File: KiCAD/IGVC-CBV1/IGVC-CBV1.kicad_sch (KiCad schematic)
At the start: 42 parts, among them IC1 SPX3819M5-L-3-3_TR, IC1 STM32F407ZGT6, IC3 AT45DB081E-SSHN-B, J1 12401948E412A, J1 STLINKV2 PINS (2.54mm Pitch), J2 Motor Driver Pins (2.54mm Pit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, J4 Conn_01x02, SW1 SW_SPDT, Y1 EB2532YA12-25.000M_TR

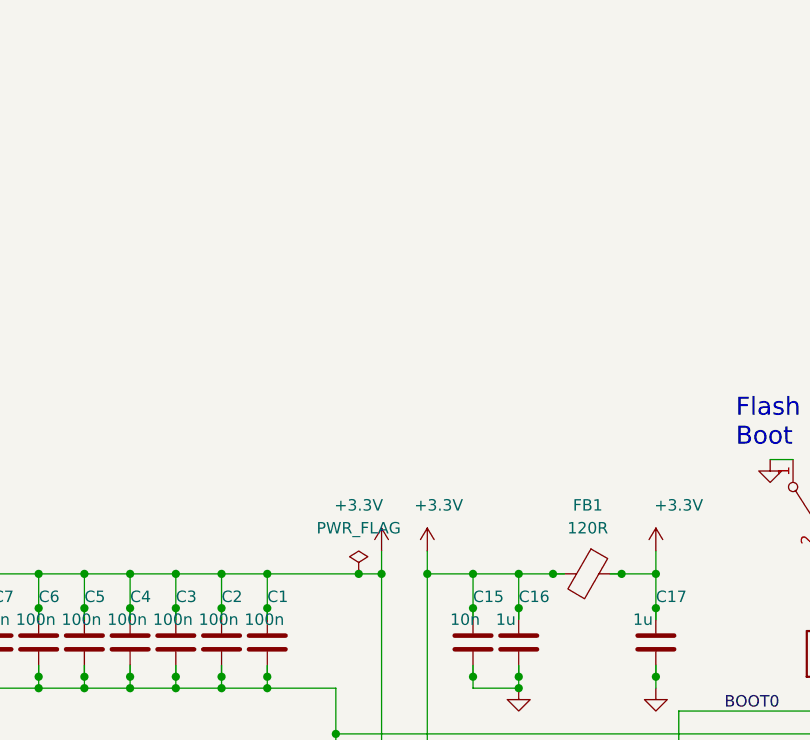
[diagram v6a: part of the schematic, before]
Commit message: Finished PCB Traces
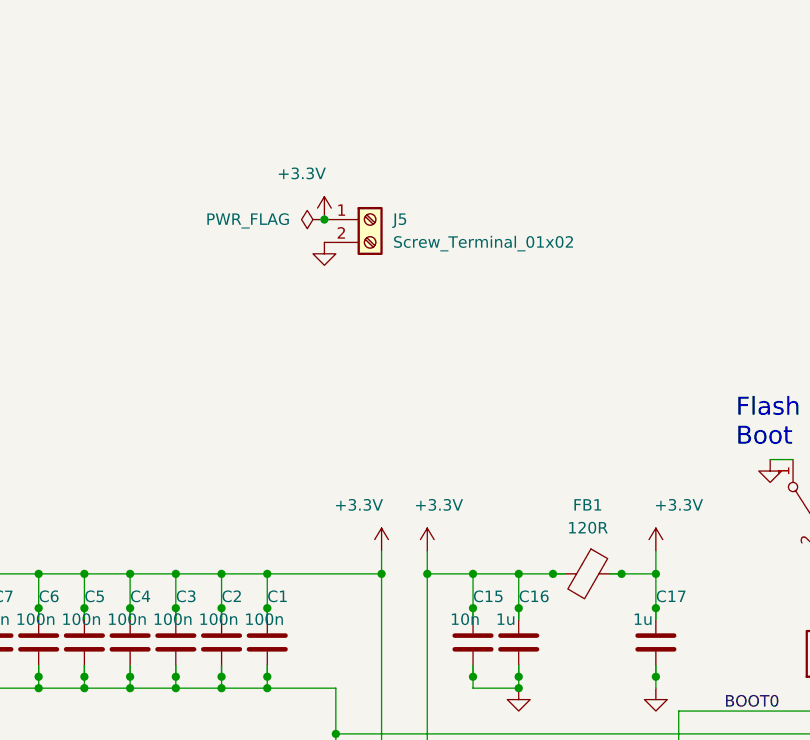
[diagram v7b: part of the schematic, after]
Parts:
- added J5: Screw_Terminal_01x02, Connector_Phoenix_MSTB:PhoenixContact_MSTBA_2,5_2-G_1x02_P5.00mm_Horizontal, symbol Connector:Screw_Terminal_01x02
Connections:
- net +3.3V: now also J5.1 (Pin_1)
- net GND: now also J5.2 (Pin_2)
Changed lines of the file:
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@@
   (junction (at 283.21 109.22) (diameter 0) (color 0 0 0 0)
   )
-  (junction (at 323.85 109.22) (diameter 0) (color 0 0 0 0)
-  )
   (junction (at 267.97 113.03) (diameter 0) (color 0 0 0 0)
   )
@@
   (junction (at 257.81 121.92) (diameter 0) (color 0 0 0 0)
   )
+  (junction (at 320.04 69.85) (diameter 0) (color 0 0 0 0)
+  )
   (junction (at 326.39 132.08) (diameter 0) (color 0 0 0 0)
   )
@@
     (stroke (width 0) (type default))
   )
-  (wire (pts (xy 313.69 109.22) (xy 323.85 109.22))
+  (wire (pts (xy 313.69 109.22) (xy 326.39 109.22))
     (stroke (width 0) (type default))
   )
@@
     (stroke (width 0) (type default))
   )
-  (wire (pts (xy 323.85 109.22) (xy 326.39 109.22))
-    (stroke (width 0) (type default))
-  )
   (wire (pts (xy 106.68 85.09) (xy 106.68 88.9))
     (stroke (width 0) (type default))
@@
     )
   )
+  (symbol (lib_id "power:PWR_FLAG") (at 320.04 69.85 90) (unit 1)
+    (in_bom yes) (on_board yes) (dnp no) (fields_autoplaced)
+    (property "Reference" "#FLG04" (at 318.135 69.85 0)
+      (effects (font (size 1.27 1.27)) hide)
+    )
+    (property "Value" "PWR_FLAG" (at 316.23 69.85 90)
+      (effects (font (size 1.27 1.27)) (justify left))
+    )
+    (property "Footprint" "" (at 320.04 69.85 0)
+      (effects (font (size 1.27 1.27)) hide)
+    )
+    (property "Datasheet" "~" (at 320.04 69.85 0)
+      (effects (font (size 1.27 1.27)) hide)
+    )
+    (pin "1")
+    (instances
+      (project "IGVC-CBV1"
+        (path "/c1e6e0fc-6008-46c6-a177-6e4d31d6ddb3"
+          (reference "#FLG04") (unit 1)
+        )
+      )
+    )
+  )
   (symbol (lib_id "power:GND") (at 107.95 158.75 0) (unit 1)
     (in_bom yes) (on_board yes) (dnp no) (fields_autoplaced)
@@
     )
   )
+  (symbol (lib_id "Connector:Screw_Terminal_01x02") (at 325.12 69.85 0) (unit 1)
+    (in_bom yes) (on_board yes) (dnp no) (fields_autoplaced)
+    (property "Reference" "J5" (at 327.66 69.85 0)
+      (effects (font (size 1.27 1.27)) (justify left))
+    )
+    (property "Value" "Screw_Terminal_01x02" (at 327.66 72.39 0)
+      (effects (font (size 1.27 1.27)) (justify left))
+    )
+    (property "Footprint" "Connector_Phoenix_MSTB:PhoenixContact_MSTBA_2,5_2-G_1x02_P5.00mm_Horizontal" (at 325.12 69.85 0)
+      (effects (font (size 1.27 1.27)) hide)
+    )
+    (property "Datasheet" "~" (at 325.12 69.85 0)
+      (effects (font (size 1.27 1.27)) hide)
+    )
+    (pin "1")
+    (pin "2")
+    (instances
+      (project "IGVC-CBV1"
+        (path "/c1e6e0fc-6008-46c6-a177-6e4d31d6ddb3"
+          (reference "J5") (unit 1)
+        )
+      )
+    )
+  )
   (symbol (lib_id "Connector_Generic:Conn_01x02") (at 166.37 157.48 90) (unit 1)
     (in_bom yes) (on_board yes) (dnp no)
@@
     )
   )
+  (symbol (lib_id "power:+3.3V") (at 320.04 69.85 0) (unit 1)
+    (in_bom yes) (on_board yes) (dnp no)
+    (property "Reference" "#PWR02" (at 320.04 73.66 0)
+      (effects (font (size 1.27 1.27)) hide)
+    )
+    (property "Value" "+3.3V" (at 317.5 64.77 0)
+      (effects (font (size 1.27 1.27)))
+    )
+    (property "Footprint" "" (at 320.04 69.85 0)
+      (effects (font (size 1.27 1.27)) hide)
+    )
+    (property "Datasheet" "" (at 320.04 69.85 0)
+      (effects (font (size 1.27 1.27)) hide)
+    )
+    (pin "1")
+    (instances
+      (project "IGVC_PCB"
+        (path "/ba927162-b9f6-45a7-80b2-ebd881f388a6"
+          (reference "#PWR02") (unit 1)
+        )
+      )
+      (project "IGVC-CBV1"
+        (path "/c1e6e0fc-6008-46c6-a177-6e4d31d6ddb3"
+          (reference "#PWR028") (unit 1)
+        )
+      )
+    )
+  )
   (symbol (lib_id "Device:C") (at 356.87 116.84 0) (unit 1)
     (in_bom yes) (on_board yes) (dnp no)
@@
     )
   )
+  (symbol (lib_id "power:GND") (at 320.04 72.39 0) (unit 1)
+    (in_bom yes) (on_board yes) (dnp no) (fields_autoplaced)
+    (property "Reference" "#PWR09" (at 320.04 78.74 0)
+      (effects (font (size 1.27 1.27)) hide)
+    )
+    (property "Value" "GND" (at 320.04 77.47 0)
+      (effects (font (size 1.27 1.27)) hide)
+    )
+    (property "Footprint" "" (at 320.04 72.39 0)
+      (effects (font (size 1.27 1.27)) hide)
+    )
+    (property "Datasheet" "" (at 320.04 72.39 0)
+      (effects (font (size 1.27 1.27)) hide)
+    )
+    (pin "1")
+    (instances
+      (project "IGVC_PCB"
+        (path "/ba927162-b9f6-45a7-80b2-ebd881f388a6"
+          (reference "#PWR09") (unit 1)
+        )
+      )
+      (project "IGVC-CBV1"
+        (path "/c1e6e0fc-6008-46c6-a177-6e4d31d6ddb3"
+          (reference "#PWR029") (unit 1)
+        )
+      )
+    )
+  )
   (symbol (lib_id "power:GND") (at 321.31 271.78 0) (unit 1)
     (in_bom yes) (on_board yes) (dnp no) (fields_autoplaced)
@@
         )
       )
-    )
-  )
-  (symbol (lib_id "power:PWR_FLAG") (at 323.85 109.22 0) (unit 1)
-    (in_bom yes) (on_board yes) (dnp no) (fields_autoplaced)
-    (property "Reference" "#FLG02" (at 323.85 107.315 0)
-      (effects (font (size 1.27 1.27)) hide)
-    )
-    (property "Value" "PWR_FLAG" (at 323.85 104.14 0)
-      (effects (font (size 1.27 1.27)))
-    )
-    (property "Footprint" "" (at 323.85 109.22 0)
-      (effects (font (size 1.27 1.27)) hide)
-    )
-    (property "Datasheet" "~" (at 323.85 109.22 0)
-      (effects (font (size 1.27 1.27)) hide)
-    )
-    (pin "1")
-    (instances
-      (project "IGVC-CBV1"
-        (path "/c1e6e0fc-6008-46c6-a177-6e4d31d6ddb3"
-          (reference "#FLG02") (unit 1)
-        )
-      )

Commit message: PCB Update
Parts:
- removed C21: 1uF, LIB_GRMMDXR60J105ME05D:CAPC0502X28N, symbol Device:C
- removed C22: .1uF, LIB_08051C104K4Z2A:CAPC2012X140N, symbol Device:C
- removed IC3: AT45DB081E-SSHN-B, LIB_AT45DB081E-SSHN-B:SOIC127P600X175-8N, symbol AT45DB081E-SSHN-B:AT45DB081E-SSHN-B
- removed R5, R6, R7: 0 Ohm, LIB_ERJ-1GJ0R00C:ERJ1G_1023, symbol Device:R_US
- removed R8: 10k, RC0402FR-0710KL:RESC1005X40N, symbol Device:R_US
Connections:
- net SPI3_MISO: no longer names the net of IC1.112 (PC11)
- net SPI3_MOSI: no longer names the net of IC1.113 (PC12)
- net SPI3_NSS: no longer names the net of IC1.40 (PA4)
- net SPI3_SCK: no longer names the net of IC1.111 (PC10)
- no-connect marks 115 -> 117
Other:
- note removed: "8 MB NOR SPI Flash"
- note removed: "LAST Thing: E-Stop. Need to create a way for the EStop to manipulate motor driver w/o MCU processing. This ensures analog intervention as opposed to fluky digital processsing teliing the motors to stop."
- moved on the sheet: J5
